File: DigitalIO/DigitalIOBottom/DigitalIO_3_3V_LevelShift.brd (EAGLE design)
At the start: 64 x 82 mm, 76 parts, among them IC1 MCP23017SP, IC2 ULN2803A, K5 HF46105, K6 HF46105, K7 HF46105, K8 HF46105, P1 DF11-06-2DS, Q1 BS170, Q2 BS170, Q5 691131710002, Q6 691131710002, Q7 691131710002, Q8 691131710002, X1 691131710005, X2 691131710004

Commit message: Add ground planes. Prepare for production.
Signed-off-by: Alexander Falkenstern <alexander.falkenstern@gmail.com>
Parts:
- C1, C2: device capacitor-wima:C2.5-3 -> rcl:C0805
- moved S1 14.5 mm to (37.0, 54.8)
- moved R22 10.1 mm to (41.4, 47.1), turned to 270 degrees
- moved C2 3.04 mm to (29.5, 50.2), flipped to the bottom, turned to 180 degrees
- moved R20 2.59 mm to (41.4, 50.9), turned to 90 degrees
- moved R21 2.52 mm to (39.8, 49.7), turned to 90 degrees
- moved SW1 0.82 mm to (48.0, 50.7)
- moved C1 0.27 mm to (26.9, 37.5), flipped to the bottom, turned to 0 degrees
- moved R14 0.06 mm to (15.2, 51.0)
- moved R27 0.05 mm to (33.0, 50.9)
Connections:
- net N$11 renamed AGND
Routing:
- net GND: track 176.3 -> 3.45 mm, vias 0 -> 118
- net AGND: track 76.5 -> 22.1 mm, vias 0 -> 46
- net +5V: track 227.0 -> 212.5 mm
- net N$57: track 23.5 -> 10.6 mm
- net N$49: track 53.6 -> 44.2 mm
- net N$31: track 29.3 -> 20.2 mm
- net N$54: track 28.6 -> 20.8 mm
- net N$55: track 59.0 -> 52.6 mm
- net N$15: track 18.9 -> 21.0 mm
- net N$37: track 33.1 -> 31.7 mm
- net N$56: track 15.5 -> 14.1 mm
- net N$43: track 38.6 -> 37.2 mm
- net N$36: track 19.1 -> 17.9 mm
- net N$42: track 22.6 -> 21.5 mm
- net N$7: track 3.55 -> 2.41 mm
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- added copper zone on layer 1, net AGND
- added copper zone on layer 1, net GND

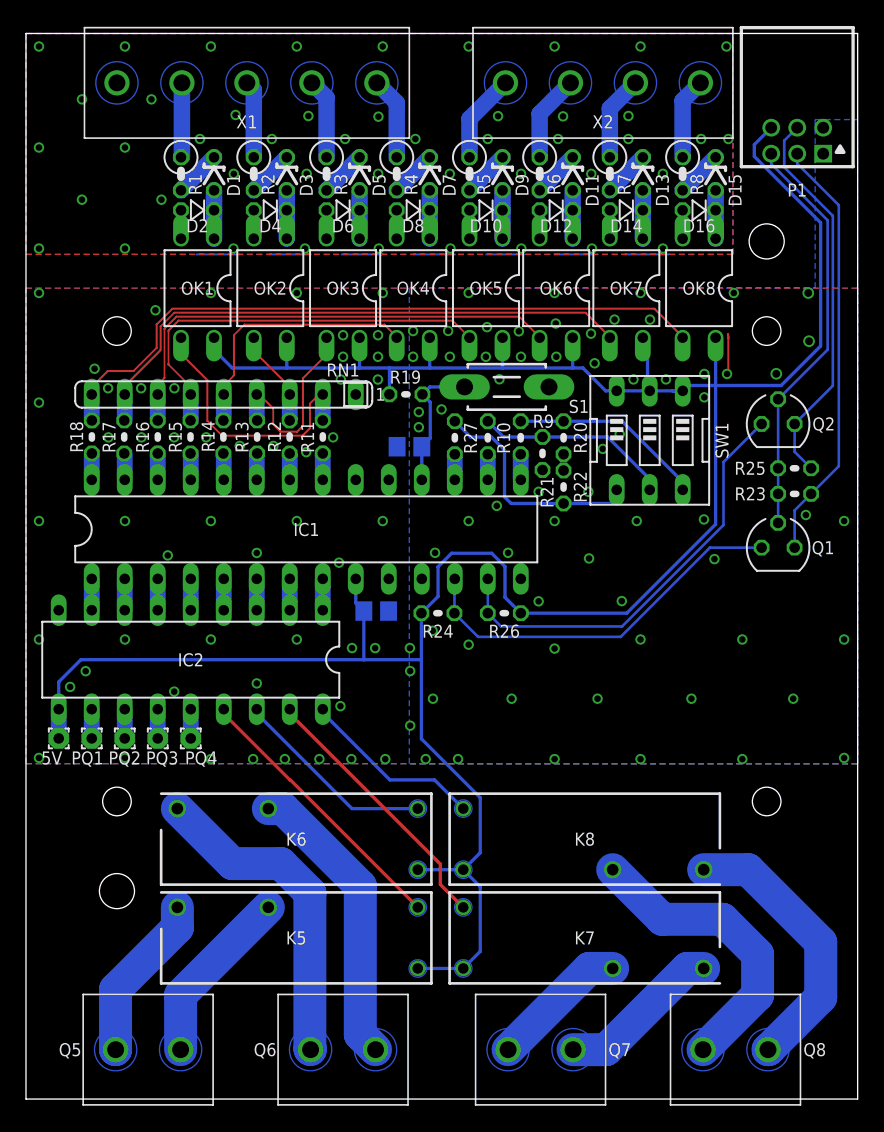
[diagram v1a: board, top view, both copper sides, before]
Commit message: Fix address selection. Increase some drills.
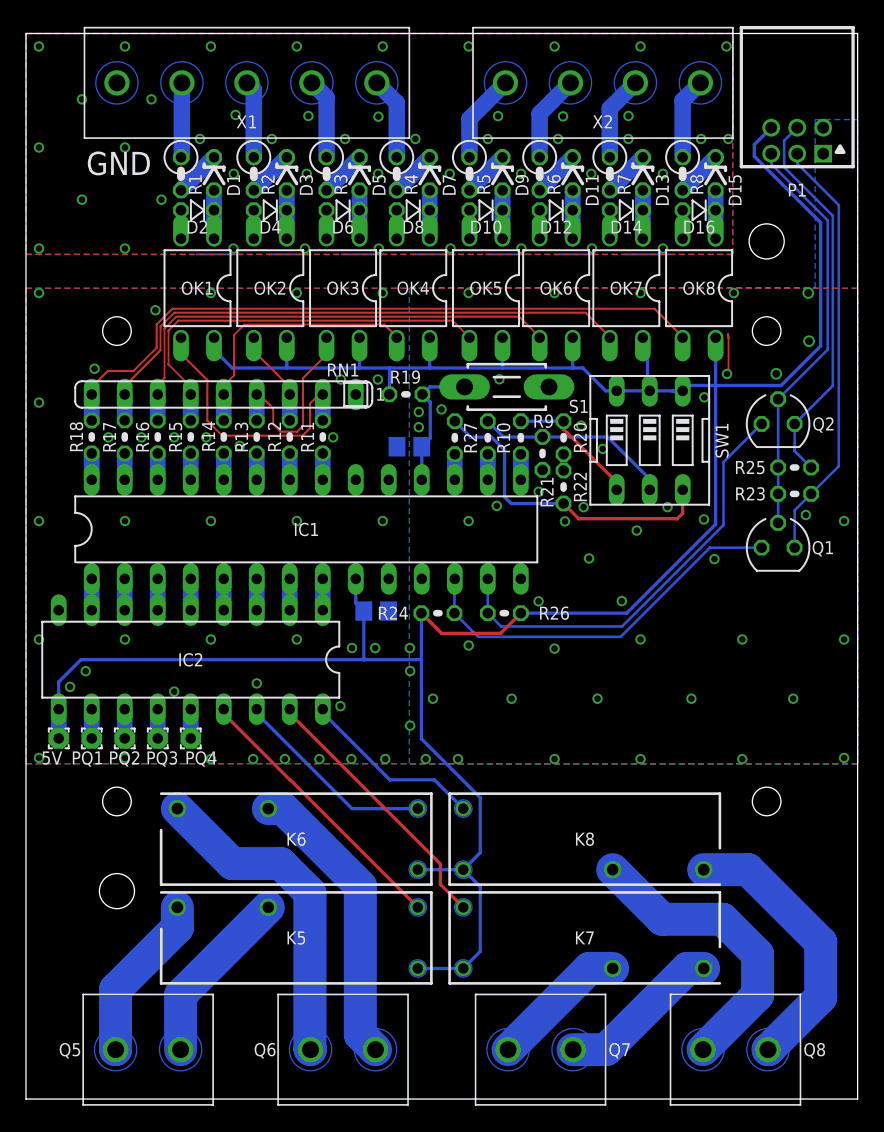
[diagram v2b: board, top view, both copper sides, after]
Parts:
- moved R25 0.06 mm to (59.1, 48.6)
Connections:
- removed net N$36: R22.2, R27.1, SW1.4
- new net N$11: R22.2, R27.1, SW1.6
- net N$77: now also SW1.4; no longer SW1.6
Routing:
- net N$11: track 0.00 -> 24.7 mm
- net N$36: track 17.9 -> 0.00 mm
- net +5V: track 212.5 -> 207.3 mm
- net N$77: track 15.0 -> 10.3 mm
- net GND: vias 118 -> 87
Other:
- board text removed: "P1"

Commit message: Add power switch and I2C interrupt wire. Add pull-up resistors for I2C. Adapt drills.
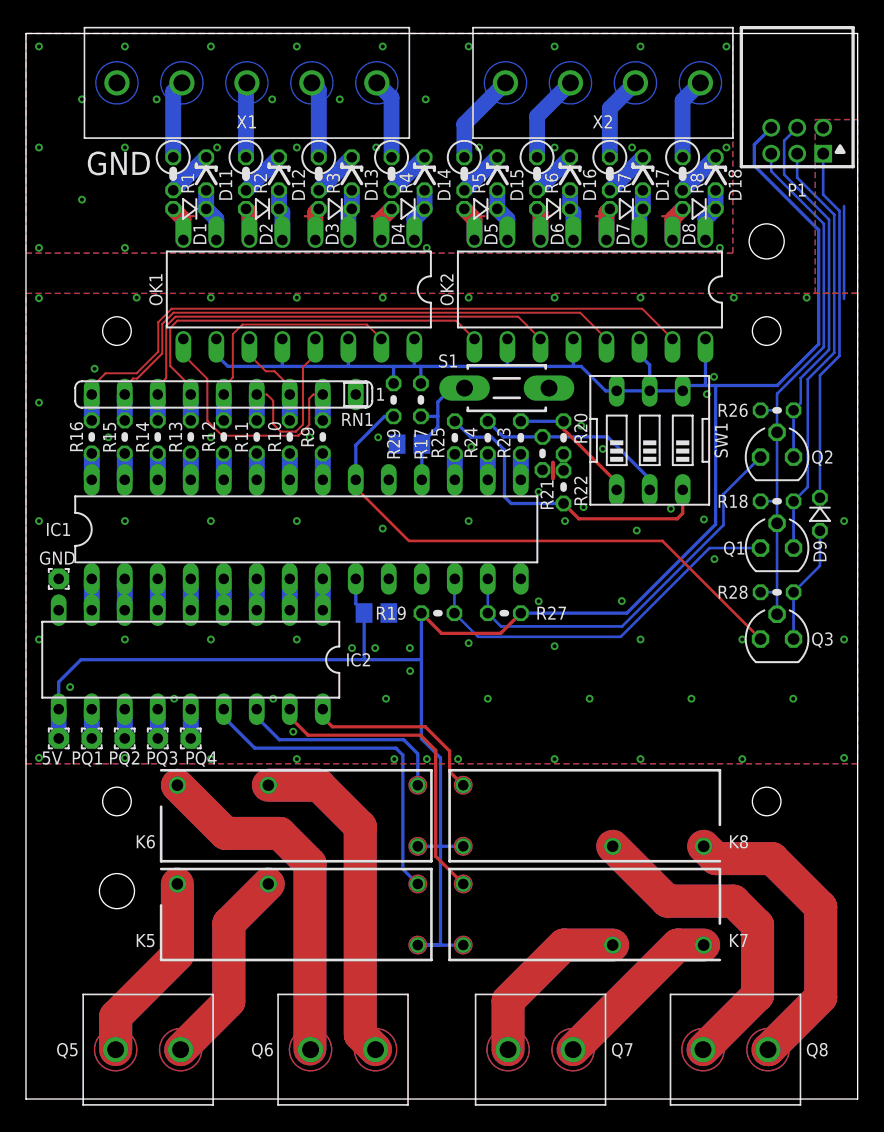
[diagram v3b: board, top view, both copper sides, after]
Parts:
- removed D10: 1N4148DO35-2V, diode:DO35-2V
- removed OK3, OK4, OK5, OK6, OK7, OK8: PC817, optocoupler:DIL04
- added D17, D18: 10V, diode:ZDIO-2.5
- added GND: WIREPAD1,6/0,8, wirepad:1,6/0,8
- added Q3: BS170, transistor-small-signal:SOT54E
- added R28, R29: 1K, rcl:0204V
- D1, D3, D5, D7, D9: value 10V -> 1N4148DO35-2V; device diode:ZDIO-2.5 -> diode:DO35-2V
- D12, D14, D16: value 1N4148DO35-2V -> 10V; device diode:DO35-2V -> diode:ZDIO-2.5
- IC1: device microchip:DIL28-3 -> mcp:DIL28-3
- OK1, OK2: value PC817 -> PC847; device optocoupler:DIL04 -> optocoupler:DIL16
- R17: value 1K -> 10K
- R18, R27: device resistor:0204V -> rcl:0204V
- R19: value 10K -> 1K; device resistor:0204V -> rcl:0204V
- R23, R24, R25: device rcl:0204V -> resistor:0204V
- moved R18 53.0 mm to (57.8, 46.0), turned to 180 degrees
- moved D9 35.8 mm to (61.1, 45.0)
- moved D11 28.2 mm to (13.9, 71.2)
- moved R25 26.3 mm to (33.0, 50.9), turned to 270 degrees
- moved R26 26.2 mm to (57.8, 53.0), turned to 180 degrees
- moved OK2 24.6 mm to (43.4, 62.3)
- moved R17 23.0 mm to (30.4, 53.8)
- moved D13 22.4 mm to (25.1, 71.2)
- moved D8 22.0 mm to (51.8, 68.5)
- moved D12 21.5 mm to (19.5, 71.2), turned to 270 degrees
- moved R23 21.5 mm to (38.1, 50.9), turned to 270 degrees
- moved R19 17.0 mm to (31.7, 37.4), turned to 0 degrees
- moved D15 16.8 mm to (36.3, 71.2)
- moved D6 16.2 mm to (40.6, 68.5)
- moved D14 15.8 mm to (30.7, 71.2), turned to 270 degrees
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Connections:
- new net N$36: D9.A, Q3.S, R28.1
- new net N$80: D9.C, P1.1
- new net N$81: IC1.20, Q3.D, R29.2
- net +3V3: now also Q3.G, R18.2, R26.2, R28.2; no longer R23.2, R25.2
- net +5V: now also OK1.10, OK1.12, OK1.14, OK1.16, OK2.10, OK2.12, OK2.14, OK2.16, R17.2, R19.1, R27.2, R29.1, SW1.4, SW1.5, SW1.6; no longer OK1.4, OK2.4, OK3.4, OK4.4, OK5.4, OK6.4, OK7.4, OK8.4, R19.2, R24.1, R26.2, SW1.1, SW1.2, SW1.3
- net AGND: now also D1.A, D3.A, D5.A, D7.A, OK1.4, OK1.6, OK1.8, OK2.4, OK2.6, OK2.8; no longer D10.A, D12.A, D14.A, D16.A, OK3.2, OK4.2, OK5.2, OK6.2, OK7.2, OK8.2
- net GND: now also GND.1
- net N$10: now also D11.C; no longer D1.C
- net N$11: now also R25.1, SW1.3; no longer R27.1, SW1.6
- net N$12: now also D1.C, D11.A, OK1.7; no longer D1.A, D2.C, OK1.1
- net N$15: now also OK1.9, R9.2; no longer OK1.3, R11.2
- net N$19: now also D12.A, D2.C, OK1.5; no longer D3.A, D4.C, OK2.1
- net N$20: now also OK1.11, R10.2; no longer OK2.3, R12.2
- net N$21: now also D13.C; no longer D5.C
- net N$23: now also D13.A, D3.C, OK1.3; no longer D5.A, D6.C, OK3.1
- net N$25: now also OK1.13, R11.2; no longer OK3.3, R13.2
- net N$27: now also D14.C; no longer D7.C
- net N$29: now also D14.A, D4.C, OK1.1; no longer D7.A, D8.C, OK4.1
- net N$31: now also OK1.15, R12.2; no longer OK4.3, R14.2
- net N$33: now also D15.C; no longer D9.C
- net N$35: now also D15.A, D5.C, OK2.7; no longer D10.C, D9.A, OK5.1
- net N$37: now also OK2.9, R13.2; no longer OK5.3, R15.2
- net N$39: now also D16.C; no longer D11.C
- net N$41: now also D16.A, D6.C, OK2.5; no longer D11.A, D12.C, OK6.1
- net N$43: now also OK2.11, R14.2; no longer OK6.3, R16.2
- net N$45: now also D17.C; no longer D13.C
- net N$47: now also D17.A, D7.C, OK2.3; no longer D13.A, D14.C, OK7.1
- net N$49: now also OK2.13, R15.2; no longer OK7.3, R17.2
- net N$50: now also R23.2; no longer R9.2
- net N$51: now also D18.C; no longer D15.C
- net N$52: now also R24.2; no longer R10.2
- net N$53: now also D18.A, D8.C, OK2.1; no longer D15.A, D16.C, OK8.1
- net N$55: now also OK2.15, R16.2; no longer OK8.3, R18.2
- net N$57: now also R17.1; no longer R19.1
- net N$58: now also R19.2; no longer R24.2
- net N$59: now also R9.1; no longer R11.1
- net N$60: now also R10.1; no longer R12.1
- net N$61: now also R27.1; no longer R26.1
- net N$62: now also R11.1; no longer R13.1
- net N$63: now also R16.1; no longer R18.1
- net N$64: now also R15.1; no longer R17.1
- net N$65: now also R14.1; no longer R16.1
- net N$67: now also R13.1; no longer R15.1
- net N$68: now also R12.1; no longer R14.1
- net N$69: now also R26.1; no longer R25.1
- net N$71: now also R18.1; no longer R23.1
- net N$77: now also R23.1, SW1.1; no longer R9.1, SW1.4
- net N$78: now also R24.1, SW1.2; no longer R10.1, SW1.5
- net N$79: now also R25.2; no longer R27.2
- net N$9: now also D12.C; no longer D3.C
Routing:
- net N$81: track 0.00 -> 43.1 mm
- net N$89: track 22.6 -> 52.1 mm
- net N$88: track 25.0 -> 53.9 mm
- net N$80: track 0.00 -> 27.6 mm
- net N$40: track 22.9 -> 50.0 mm
- net N$38: track 21.3 -> 47.2 mm
- net AGND: track 22.1 -> 46.5 mm, vias 46 -> 28
- net N$75: track 13.7 -> 31.1 mm
- net N$46: track 10.6 -> 27.2 mm
- net N$66: track 12.9 -> 29.4 mm
- net N$44: track 12.6 -> 26.8 mm
- net +3V3: track 31.8 -> 42.4 mm
- net N$36: track 0.00 -> 9.17 mm
- net GND: track 3.45 -> 9.57 mm, vias 87 -> 70
- net +5V: track 207.3 -> 202.5 mm
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- added copper zone on layer 1, net +5V
- added copper zone on layer 1, net N$38
- added copper zone on layer 1, net N$40
- added copper zone on layer 1, net N$42
- added copper zone on layer 1, net N$44
- added copper zone on layer 1, net N$46
- added copper zone on layer 1, net N$48
- added copper zone on layer 1, net N$54
- added copper zone on layer 1, net N$56
- added copper zone on layer 1, net N$66
- added copper zone on layer 1, net N$75
- added copper zone on layer 1, net N$88
- added copper zone on layer 1, net N$89
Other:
- board text added: "INT-Settings: 1. Mirror 2. Open drain"
